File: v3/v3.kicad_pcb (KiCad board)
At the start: 4 copper layers, 10 x 28.5 mm, 41 parts, among them J1 Conn_01x10_Male, Q10 MMTB3904, Q11 MMTB3904, Q12 MMTB3904, Q13 MMTB3904, Q14 MMTB3904, Q15 MMTB3904, Q16 MMTB3904, Q17 MMTB3904, Q2 MMTB3904, Q3 MMTB3904, Q4 MMTB3904, Q5 MMTB3904, Q6 MMTB3904, Q7 MMTB3904, Q8 MMTB3904, Q9 MMTB3904

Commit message: fighting with freecad and updating documentation
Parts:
- removed D3, D5, D7, D8, D9: LIST-C191K, LED_SMD:LED_0603_1608Metric
- removed J1: Conn_01x10_Male, Connector_PinHeader_2.54mm:PinHeader_1x10_P2.54mm_Vertical
- removed Q10, Q13, Q14, Q15, Q16, Q17, Q5, Q6, Q9: MMTB3904, Package_TO_SOT_SMD:SOT-23
- removed R10, R14, R16, R6: 100K, Resistor_SMD:R_0603_1608Metric
- removed R13, R15, R17, R5, R9: 100, Resistor_SMD:R_0603_1608Metric
- added D1: LIST-C191K, LED_SMD:LED_0603_1608Metric, F.Cu at (79.4, 34.7)
- added Q1: MMTB3904, Package_TO_SOT_SMD:SOT-23-3, B.Cu at (76.6, 34.8)
- added R1: 10K, Resistor_SMD:R_0603_1608Metric, F.Cu at (73.7, 34.8)
- Q11, Q3, Q7: footprint Package_TO_SOT_SMD:SOT-23 -> Package_TO_SOT_SMD:SOT-23-3; moved to B.Cu
- Q12, Q2, Q4, Q8: footprint Package_TO_SOT_SMD:SOT-23 -> Package_TO_SOT_SMD:SOT-23-3; moved to F.Cu
- R11, R3, R7: value 100 -> 10K; moved to F.Cu
- R12, R2, R4, R8: value 100K -> 100; moved to B.Cu
- moved D2 22.7 mm to (73.7, 38.3), turned to -90 degrees
- moved Q12 18.2 mm to (76.5, 45.2), turned to 0 degrees
- moved R11 17.6 mm to (73.6, 45.2)
- moved Q3 17.5 mm to (76.6, 38.3)
- moved R7 17.4 mm to (73.6, 41.8)
- moved Q11 17.3 mm to (76.5, 45.1), turned to 180 degrees
- moved Q8 17.3 mm to (76.5, 41.8), turned to 0 degrees
- moved R4 17.2 mm to (73.7, 38.3)
- moved Q7 17.0 mm to (76.5, 41.8), turned to 180 degrees
- moved D6 17.0 mm to (79.3, 45.1)
- moved Q2 16.9 mm to (76.6, 34.8), turned to 0 degrees
- moved Q4 16.9 mm to (76.6, 38.2)
- moved D4 16.7 mm to (79.3, 41.7)
- moved R12 13.3 mm to (79.3, 45.1), turned to -90 degrees
- moved R3 12.3 mm to (79.4, 38.2), turned to 90 degrees
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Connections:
- net /v+ renamed /V+
- D2 pad 1: Net-(D2-Pad1) -> Net-(D2-K)
- D4 pad 1: Net-(D4-Pad1) -> Net-(D4-K)
- D6 pad 1: Net-(D6-Pad1) -> Net-(D6-K)
- Q11 pad 1: Net-(Q10-Pad2) -> Net-(Q11-B)
- Q11 pad 2: Net-(Q10-Pad3) -> /V-
- Q11 pad 3: Net-(D6-Pad1) -> Net-(Q11-C)
- Q12 pad 1: /v- -> Net-(Q11-C)
- Q12 pad 2: Net-(Q12-Pad2) -> Net-(Q11-B)
- Q12 pad 3: Net-(Q12-Pad3) -> Net-(D6-K)
- Q2 pad 1: /v- -> Net-(Q1-C)
- Q2 pad 2: Net-(Q2-Pad2) -> Net-(Q1-B)
- Q2 pad 3: Net-(Q2-Pad3) -> Net-(D1-K)
- Q3 pad 1: Net-(Q2-Pad2) -> Net-(Q3-B)
- Q3 pad 2: Net-(Q2-Pad3) -> /V-
- Q3 pad 3: Net-(D2-Pad1) -> Net-(Q3-C)
- Q4 pad 1: /v- -> Net-(Q3-C)
- Q4 pad 2: Net-(Q4-Pad2) -> Net-(Q3-B)
- Q4 pad 3: Net-(Q4-Pad3) -> Net-(D2-K)
- Q7 pad 1: Net-(Q6-Pad2) -> Net-(Q7-B)
- Q7 pad 2: Net-(Q6-Pad3) -> /V-
- Q7 pad 3: Net-(D4-Pad1) -> Net-(Q7-C)
- Q8 pad 1: /v- -> Net-(Q7-C)
- Q8 pad 2: Net-(Q8-Pad2) -> Net-(Q7-B)
- Q8 pad 3: Net-(Q8-Pad3) -> Net-(D4-K)
- R11 pad 1: Net-(Q10-Pad2) -> Net-(Q11-C)
- R11 pad 2: /v- -> /CTRL
- R12 pad 1: Net-(Q12-Pad3) -> Net-(Q11-B)
- R12 pad 2: /c5 -> /V-
- R2 pad 1: Net-(Q2-Pad3) -> Net-(Q1-B)
- R2 pad 2: /c0 -> /V-
- R3 pad 1: Net-(Q2-Pad2) -> Net-(Q3-C)
- R3 pad 2: /v- -> /CTRL
- R4 pad 1: Net-(Q4-Pad3) -> Net-(Q3-B)
- R4 pad 2: /c1 -> /V-
- R7 pad 1: Net-(Q6-Pad2) -> Net-(Q7-C)
- R7 pad 2: /v- -> /CTRL
- R8 pad 1: Net-(Q8-Pad3) -> Net-(Q7-B)
- R8 pad 2: /c3 -> /V-
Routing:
- net /v-: track 39.2 -> 0.00 mm, vias 8 -> 0
- net /V-: track 0.00 -> 7.05 mm
- net Net-(Q12-Pad2): track 5.54 -> 0.00 mm, vias 2 -> 0
- net Net-(Q4-Pad2): track 5.52 -> 0.00 mm, vias 2 -> 0
- net Net-(Q2-Pad2): track 5.52 -> 0.00 mm, vias 2 -> 0
- net Net-(Q6-Pad2): track 5.52 -> 0.00 mm, vias 2 -> 0
- net Net-(Q10-Pad2): track 5.47 -> 0.00 mm, vias 2 -> 0
- net Net-(Q16-Pad2): track 5.47 -> 0.00 mm, vias 2 -> 0
- net /c0: track 5.42 -> 0.00 mm
- net Net-(Q8-Pad2): track 5.37 -> 0.00 mm, vias 2 -> 0
- net Net-(Q14-Pad2): track 5.37 -> 0.00 mm, vias 2 -> 0
- net Net-(Q3-B): track 0.00 -> 4.82 mm, vias 0 -> 1
- net Net-(Q1-B): track 0.00 -> 4.82 mm, vias 0 -> 1
- net Net-(Q7-B): track 0.00 -> 4.82 mm, vias 0 -> 1
- net Net-(Q11-B): track 0.00 -> 4.82 mm, vias 0 -> 1
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- removed copper zone on In1.Cu, net /V+
- removed copper zone on In2.Cu, net /v-
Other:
- board outline removed
- copper layers 4 -> 2
- net class Default removed
- rule pad_to_mask_clearance: 0 -> 0.0508
- board text removed: "LED Breadboard Module V3 2021"

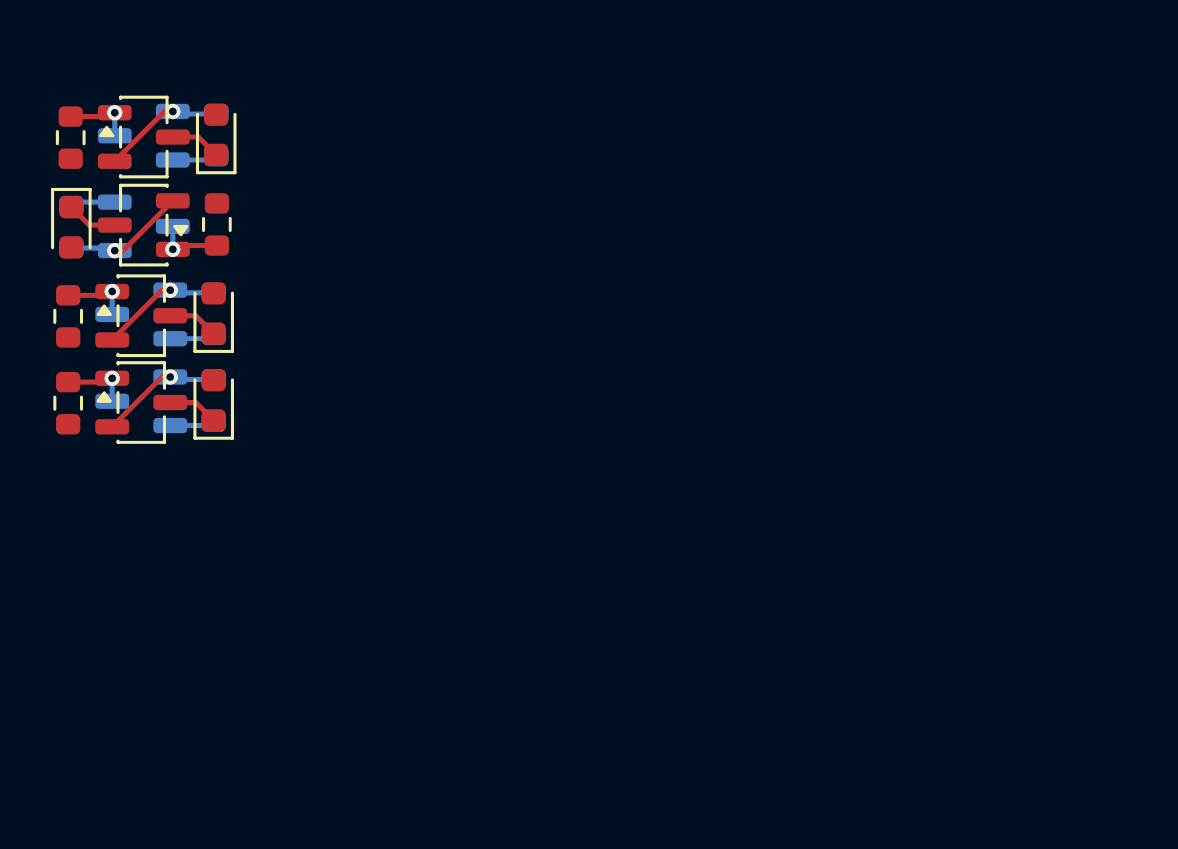
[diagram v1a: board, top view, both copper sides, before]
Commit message: feat: design a module for red/green led
a 4 pin narrow breadboard module.
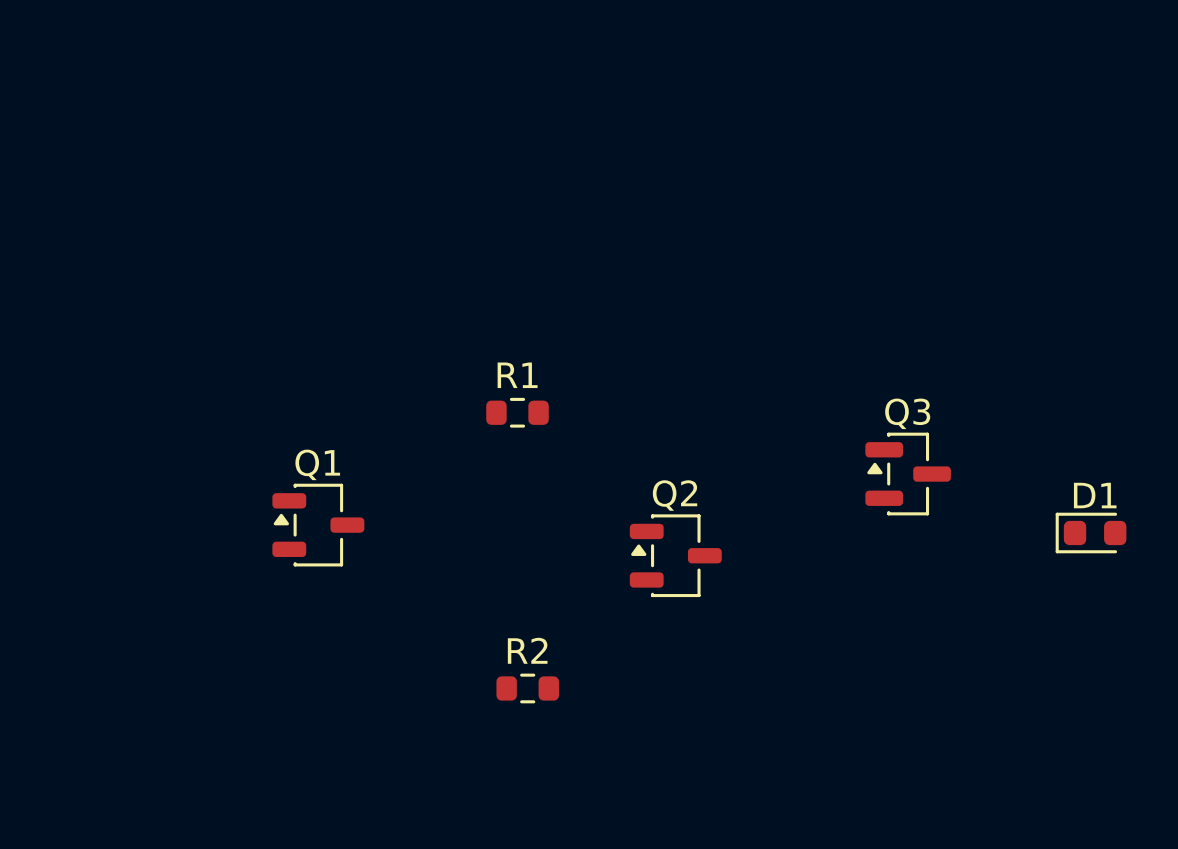
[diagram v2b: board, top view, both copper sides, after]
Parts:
- removed D2, D4, D6: LIST-C191K, LED_SMD:LED_0603_1608Metric
- removed Q11, Q12, Q4, Q7, Q8: MMTB3904, Package_TO_SOT_SMD:SOT-23-3
- removed R11, R3, R7: 10K, Resistor_SMD:R_0603_1608Metric
- removed R12, R4, R8: 100, Resistor_SMD:R_0603_1608Metric
- Q1: moved to F.Cu
- Q3: value MMTB3904 -> BSS138; footprint Package_TO_SOT_SMD:SOT-23-3 -> Package_TO_SOT_SMD:SOT-23; moved to F.Cu
- R2: value 100 -> 68; moved to F.Cu
- moved D1 37.8 mm to (113.8, 50.3), turned to 0 degrees
- moved Q3 31.5 mm to (106.5, 48.0)
- moved Q2 26.5 mm to (97.4, 51.2)
- moved R2 24.9 mm to (91.6, 56.4), turned to 0 degrees
- moved R1 20.6 mm to (91.2, 45.6), turned to 0 degrees
- moved Q1 16.7 mm to (83.4, 50.0), turned to 0 degrees
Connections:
- Q2 pad 2: Net-(Q1-B) -> Net-(Q2-E)
- Q3 pad 1: Net-(Q3-B) -> /CTRL
- Q3 pad 2: /V- -> Net-(Q1-B)
- Q3 pad 3: Net-(Q3-C) -> Net-(Q2-E)
- R1 pad 2: /CTRL -> /V+
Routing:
- net /V-: track 7.05 -> 0.00 mm
- net Net-(Q3-B): track 4.82 -> 0.00 mm, vias 1 -> 0
- net Net-(Q1-B): track 4.82 -> 0.00 mm, vias 1 -> 0
- net Net-(Q7-B): track 4.82 -> 0.00 mm, vias 1 -> 0
- net Net-(Q11-B): track 4.82 -> 0.00 mm, vias 1 -> 0
- net Net-(Q3-C): track 2.69 -> 0.00 mm, vias 1 -> 0
- net Net-(Q7-C): track 2.69 -> 0.00 mm, vias 1 -> 0
- net Net-(Q11-C): track 2.69 -> 0.00 mm, vias 1 -> 0
- net Net-(Q1-C): track 2.69 -> 0.00 mm, vias 1 -> 0
- net Net-(D4-K): track 1.99 -> 0.00 mm
- net Net-(D2-K): track 1.99 -> 0.00 mm
- net Net-(D1-K): track 1.99 -> 0.00 mm
- net Net-(D6-K): track 1.99 -> 0.00 mm
